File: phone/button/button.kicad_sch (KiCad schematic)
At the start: 2 parts, among them J1 Conn_01x02, SW1 SW_Push

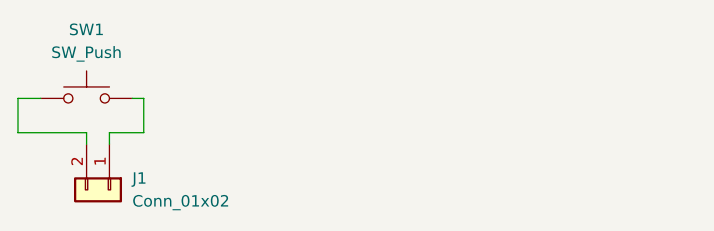
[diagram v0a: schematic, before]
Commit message: edited switch pcb and made buttons, add speaker grill , add switch pcb support
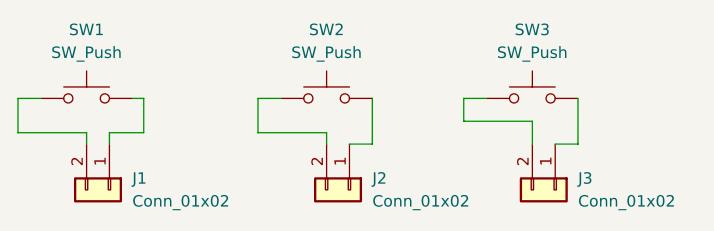
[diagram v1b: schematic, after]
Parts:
- added J2, J3: Conn_01x02, solderwirepad_1_02_SMD:SolderWirePad_1x02_SMD_5x5mm, symbol Connector_Generic:Conn_01x02
- added SW2, SW3: SW_Push, Button_Switch_THT:SW_PUSH_6mm, symbol Switch:SW_Push
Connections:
- new net: J2.2 (Pin_2), SW2.1
- new net: J2.1 (Pin_1), SW2.2
- new net: J3.2 (Pin_2), SW3.1
- new net: J3.1 (Pin_1), SW3.2
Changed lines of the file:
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@@
 (kicad_sch (version 20211123) (generator eeschema)
   (paper "A4")
+  (wire (pts (xy 124.46 66.04) (xy 124.46 69.85))
+    (stroke (width 0) (type default) (color 0 0 0 0))
+  )
+  (wire (pts (xy 127 66.04) (xy 124.46 66.04))
+    (stroke (width 0) (type default) (color 0 0 0 0))
+  )
   (wire (pts (xy 110.49 66.04) (xy 111.76 66.04))
     (stroke (width 0) (type default) (color 0 0 0 0))
   )
   (wire (pts (xy 97.79 69.85) (xy 105.41 69.85))
+    (stroke (width 0) (type default) (color 0 0 0 0))
+  )
+  (wire (pts (xy 160.02 66.04) (xy 160.02 71.12))
+    (stroke (width 0) (type default) (color 0 0 0 0))
+  )
+  (wire (pts (xy 154.94 68.58) (xy 154.94 71.12))
+    (stroke (width 0) (type default) (color 0 0 0 0))
+  )
+  (wire (pts (xy 149.86 66.04) (xy 147.32 66.04))
     (stroke (width 0) (type default) (color 0 0 0 0))
   )
@@
     (stroke (width 0) (type default) (color 0 0 0 0))
   )
+  (wire (pts (xy 157.48 71.12) (xy 160.02 71.12))
+    (stroke (width 0) (type default) (color 0 0 0 0))
+  )
+  (wire (pts (xy 147.32 66.04) (xy 147.32 68.58))
+    (stroke (width 0) (type default) (color 0 0 0 0))
+  )
+  (wire (pts (xy 124.46 69.85) (xy 132.08 69.85))
+    (stroke (width 0) (type default) (color 0 0 0 0))
+  )
+  (wire (pts (xy 132.08 69.85) (xy 132.08 71.12))
+    (stroke (width 0) (type default) (color 0 0 0 0))
+  )
+  (wire (pts (xy 137.16 66.04) (xy 137.16 71.12))
+    (stroke (width 0) (type default) (color 0 0 0 0))
+  )
+  (wire (pts (xy 147.32 68.58) (xy 154.94 68.58))
+    (stroke (width 0) (type default) (color 0 0 0 0))
+  )
   (wire (pts (xy 111.76 69.85) (xy 107.95 69.85))
     (stroke (width 0) (type default) (color 0 0 0 0))
+  )
+  (wire (pts (xy 137.16 71.12) (xy 134.62 71.12))
+    (stroke (width 0) (type default) (color 0 0 0 0))
+  )
+  (symbol (lib_id "Switch:SW_Push") (at 132.08 66.04 0) (unit 1)
+    (in_bom yes) (on_board yes) (fields_autoplaced)
+    (property "Reference" "SW2" (id 0) (at 132.08 58.42 0))
+    (property "Value" "SW_Push" (id 1) (at 132.08 60.96 0))
+    (property "Footprint" "Button_Switch_THT:SW_PUSH_6mm" (id 2) (at 132.08 60.96 0)
+      (effects (font (size 1.27 1.27)) hide)
+    )
+    (property "Datasheet" "~" (id 3) (at 132.08 60.96 0)
+      (effects (font (size 1.27 1.27)) hide)
+    )
+    (pin "1")
+    (pin "2")
+  )
+  (symbol (lib_id "Connector_Generic:Conn_01x02") (at 134.62 76.2 270) (unit 1)
+    (in_bom yes) (on_board yes) (fields_autoplaced)
+    (property "Reference" "J2" (id 0) (at 137.16 74.9299 90)
+      (effects (font (size 1.27 1.27)) (justify left))
+    )
+    (property "Value" "Conn_01x02" (id 1) (at 137.16 77.4699 90)
+      (effects (font (size 1.27 1.27)) (justify left))
+    )
+    (property "Footprint" "solderwirepad_1_02_SMD:SolderWirePad_1x02_SMD_5x5mm" (id 2) (at 134.62 76.2 0)
+      (effects (font (size 1.27 1.27)) hide)
+    )
+    (property "Datasheet" "~" (id 3) (at 134.62 76.2 0)
+      (effects (font (size 1.27 1.27)) hide)
+    )
+    (pin "1")
+    (pin "2")
+  )
+  (symbol (lib_id "Switch:SW_Push") (at 154.94 66.04 0) (unit 1)
+    (in_bom yes) (on_board yes) (fields_autoplaced)
+    (property "Reference" "SW3" (id 0) (at 154.94 58.42 0))
+    (property "Value" "SW_Push" (id 1) (at 154.94 60.96 0))
+    (property "Footprint" "Button_Switch_THT:SW_PUSH_6mm" (id 2) (at 154.94 60.96 0)
+      (effects (font (size 1.27 1.27)) hide)
+    )
+    (property "Datasheet" "~" (id 3) (at 154.94 60.96 0)
+      (effects (font (size 1.27 1.27)) hide)
+    )
+    (pin "1")
+    (pin "2")
   )
   (symbol (lib_id "Connector_Generic:Conn_01x02") (at 107.95 76.2 270) (unit 1)
@@
     )
     (property "Datasheet" "~" (id 3) (at 107.95 76.2 0)
+      (effects (font (size 1.27 1.27)) hide)
+    )
+    (pin "1")
+    (pin "2")
+  )
+  (symbol (lib_id "Connector_Generic:Conn_01x02") (at 157.48 76.2 270) (unit 1)
+    (in_bom yes) (on_board yes) (fields_autoplaced)
+    (property "Reference" "J3" (id 0) (at 160.02 74.9299 90)
+      (effects (font (size 1.27 1.27)) (justify left))
+    )
+    (property "Value" "Conn_01x02" (id 1) (at 160.02 77.4699 90)
+      (effects (font (size 1.27 1.27)) (justify left))
+    )
+    (property "Footprint" "solderwirepad_1_02_SMD:SolderWirePad_1x02_SMD_5x5mm" (id 2) (at 157.48 76.2 0)
+      (effects (font (size 1.27 1.27)) hide)
+    )
+    (property "Datasheet" "~" (id 3) (at 157.48 76.2 0)
       (effects (font (size 1.27 1.27)) hide)
     )
@@
       (reference "J1") (unit 1) (value "Conn_01x02") (footprint "solderwirepad_1_02_SMD:SolderWirePad_1x02_SMD_5x5mm")
     )
+    (path "/59820597-7189-45d5-a801-ad1518327972"
+      (reference "J2") (unit 1) (value "Conn_01x02") (footprint "solderwirepad_1_02_SMD:SolderWirePad_1x02_SMD_5x5mm")
+    )
+    (path "/cbac1f46-3c97-47a3-b093-e7139b883825"
+      (reference "J3") (unit 1) (value "Conn_01x02") (footprint "solderwirepad_1_02_SMD:SolderWirePad_1x02_SMD_5x5mm")
+    )
     (path "/ed2e4d61-59eb-4b89-971a-0902c4a32548"
       (reference "SW1") (unit 1) (value "SW_Push") (footprint "Button_Switch_THT:SW_PUSH_6mm")
     )
+    (path "/510f7c5c-4931-4a03-bb52-806933528374"
+      (reference "SW2") (unit 1) (value "SW_Push") (footprint "Button_Switch_THT:SW_PUSH_6mm")
+    )
+    (path "/644dda17-c33b-4d94-95b0-fff7d75a8de7"
+      (reference "SW3") (unit 1) (value "SW_Push") (footprint "Button_Switch_THT:SW_PUSH_6mm")
+    )
   )
